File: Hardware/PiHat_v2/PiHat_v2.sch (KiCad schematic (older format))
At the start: 31 parts, among them P1 CONN_02X20, P2 CONN_01X02, P3 CONN_01X08

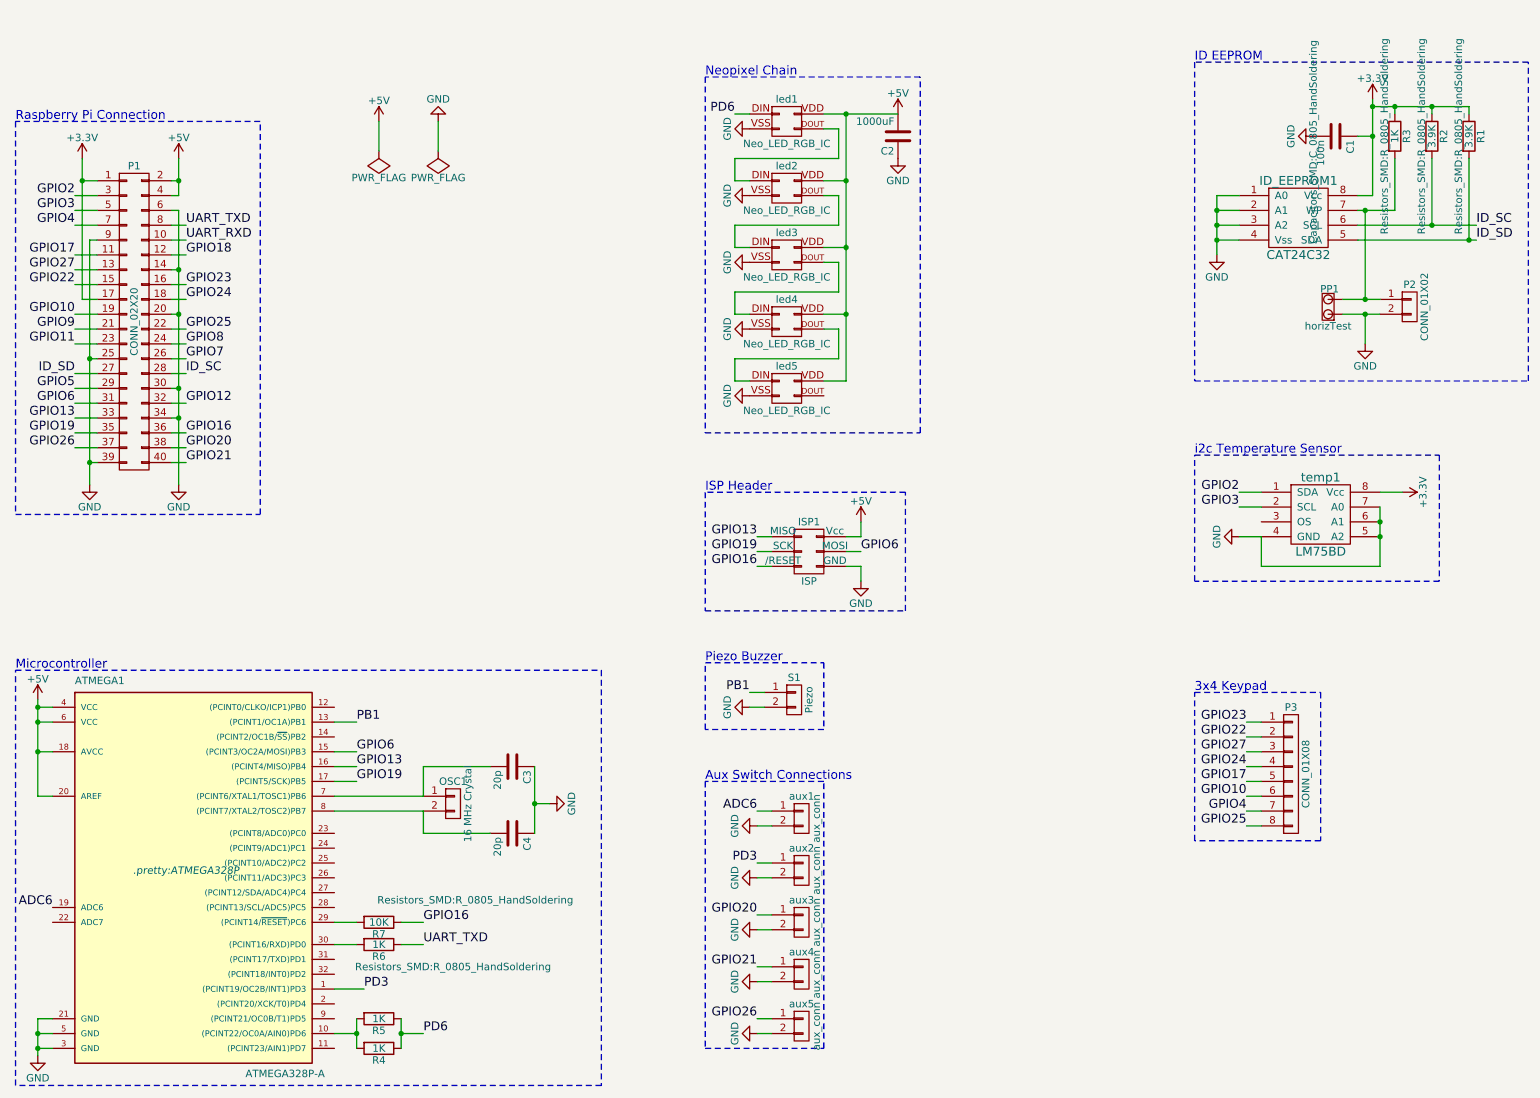
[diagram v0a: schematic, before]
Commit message: Take AREF off 5v for ATMEGA
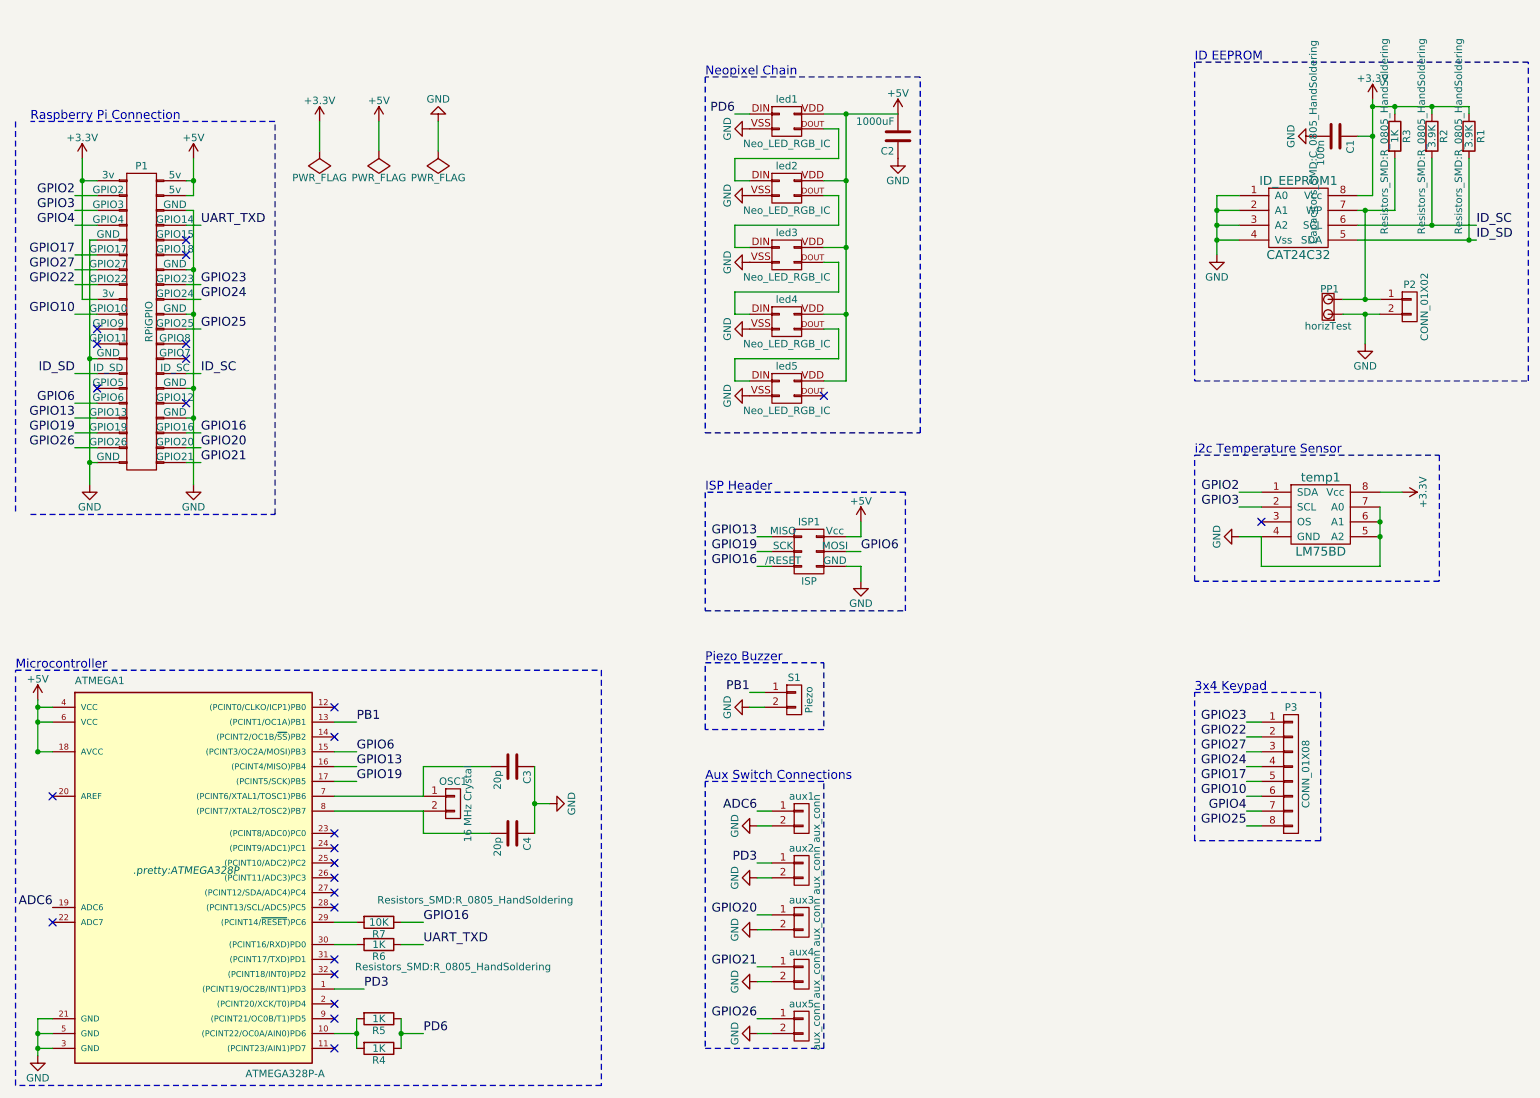
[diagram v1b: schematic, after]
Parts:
- removed P1: CONN_02X20, Pin_Headers:Pin_Header_Straight_2x20_Pitch2.54mm, symbol CONN_02X20
- added P1: RPiGPIO, symbol RPiGPIO
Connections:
- net +3V3: now also P1.1 (3v), P1.17 (3v)
- net +5V: now also P1.2 (5v), P1.4 (5v); no longer ATMEGA1.20 (AREF)
- net GND: now also P1.14 (GND), P1.20 (GND), P1.25 (GND), P1.30 (GND), P1.34 (GND), P1.39 (GND), P1.6 (GND), P1.9 (GND)
- net GPIO10: now also P1.19 (GPIO10)
- net GPIO13: now also P1.33 (GPIO13)
- net GPIO16: now also P1.36 (GPIO16)
- net GPIO17: now also P1.11 (GPIO17)
- net GPIO19: now also P1.35 (GPIO19)
- net GPIO2: now also P1.3 (GPIO2)
- net GPIO20: now also P1.38 (GPIO20)
- net GPIO21: now also P1.40 (GPIO21)
- net GPIO22: now also P1.15 (GPIO22)
- net GPIO23: now also P1.16 (GPIO23)
- net GPIO24: now also P1.18 (GPIO24)
- net GPIO25: now also P1.22 (GPIO25)
- net GPIO26: now also P1.37 (GPIO26)
- net GPIO27: now also P1.13 (GPIO27)
- net GPIO3: now also P1.5 (GPIO3)
- net GPIO4: now also P1.7 (GPIO4)
- net GPIO6: now also P1.31 (GPIO6)
- net ID_SC: now also P1.28 (ID_SC)
- net ID_SD: now also P1.27 (ID_SD)
- net UART_TXD: now also P1.8 (GPIO14)
- no-connect marks 0 -> 25
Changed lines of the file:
@@
 $EndDescr
-$Comp
-L CONN_02X20 P1
-U 1 1 588857EE
-P 1550 2500
-F 0 "P1" H 1550 3550 50  0000 C CNN
-F 1 "CONN_02X20" V 1550 2500 50  0000 C CNN
-F 2 "Pin_Headers:Pin_Header_Straight_2x20_Pitch2.54mm" H 1550 1550 50  0001 C CNN
-F 3 "" H 1550 1550 50  0000 C CNN
-	1    1550 2500
-	1    0    0    -1
-$EndComp
 $Comp
 L +3.3V #PWR01
@@
 L +5V #PWR02
 U 1 1 58885909
-P 1850 1400
-F 0 "#PWR02" H 1850 1250 50  0001 C CNN
-F 1 "+5V" H 1850 1540 50  0000 C CNN
-F 2 "" H 1850 1400 50  0000 C CNN
-F 3 "" H 1850 1400 50  0000 C CNN
-	1    1850 1400
+P 1950 1400
+F 0 "#PWR02" H 1950 1250 50  0001 C CNN
+F 1 "+5V" H 1950 1540 50  0000 C CNN
+F 2 "" H 1950 1400 50  0000 C CNN
+F 3 "" H 1950 1400 50  0000 C CNN
+	1    1950 1400
 	1    0    0    -1
 $EndComp
@@
 L GND #PWR03
 U 1 1 58885944
-P 1850 3600
-F 0 "#PWR03" H 1850 3350 50  0001 C CNN
-F 1 "GND" H 1850 3450 50  0000 C CNN
-F 2 "" H 1850 3600 50  0000 C CNN
-F 3 "" H 1850 3600 50  0000 C CNN
-	1    1850 3600
+P 1950 3600
+F 0 "#PWR03" H 1950 3350 50  0001 C CNN
+F 1 "GND" H 1950 3450 50  0000 C CNN
+F 2 "" H 1950 3600 50  0000 C CNN
+F 3 "" H 1950 3600 50  0000 C CNN
+	1    1950 3600
 	1    0    0    -1
 $EndComp
@@
 Text Label 1150 2450 2    60   ~ 0
 GPIO10
-Text Label 1150 2550 2    60   ~ 0
-GPIO9
-Text Label 1150 2650 2    60   ~ 0
-GPIO11
 Text Label 1150 2850 2    60   ~ 0
 ID_SD
-Text Label 1150 2950 2    60   ~ 0
-GPIO5
 Text Label 1150 3050 2    60   ~ 0
 GPIO6
@@
 Text Label 1150 3350 2    60   ~ 0
 GPIO26
-Text Label 1900 3450 0    60   ~ 0
+Text Label 2000 3450 0    60   ~ 0
 GPIO21
-Text Label 1900 3350 0    60   ~ 0
+Text Label 2000 3350 0    60   ~ 0
 GPIO20
-Text Label 1900 3250 0    60   ~ 0
+Text Label 2000 3250 0    60   ~ 0
 GPIO16
-Text Label 1900 3050 0    60   ~ 0
-GPIO12
-Text Label 1900 2850 0    60   ~ 0
+Text Label 2000 2850 0    60   ~ 0
 ID_SC
-Text Label 1900 2750 0    60   ~ 0
-GPIO7
-Text Label 1900 2650 0    60   ~ 0
-GPIO8
-Text Label 1900 2550 0    60   ~ 0
+Text Label 2000 2550 0    60   ~ 0
 GPIO25
-Text Label 1900 2350 0    60   ~ 0
+Text Label 2000 2350 0    60   ~ 0
 GPIO24
-Text Label 1900 2250 0    60   ~ 0
+Text Label 2000 2250 0    60   ~ 0
 GPIO23
-Text Label 1900 2050 0    60   ~ 0
-GPIO18
-Text Label 1900 1950 0    60   ~ 0
-UART_RXD
-Text Label 1900 1850 0    60   ~ 0
+Text Label 2000 1850 0    60   ~ 0
 UART_TXD
-Text Notes 750  1150 0    60   ~ 0
+Text Notes 850  1150 0    60   ~ 0
 Raspberry Pi Connection
 $Comp
@@
 	1000 7300 900  7300
 Connection ~ 900  5400
-Wire Wire Line
-	900  5700 1000 5700
 Connection ~ 900  5100
 Wire Wire Line
 	900  5400 1000 5400
-Wire Wire Line
-	900  5050 900  5700
 Wire Wire Line
 	1000 5100 900  5100
@@
 Wire Wire Line
 	1250 3450 1300 3450
-Connection ~ 1850 3150
-Connection ~ 1850 2950
-Connection ~ 1850 2450
-Connection ~ 1850 2150
-Wire Wire Line
-	1850 1750 1850 3600
-Wire Wire Line
-	1850 1750 1800 1750
-Wire Wire Line
-	1850 2150 1800 2150
-Wire Wire Line
-	1850 2450 1800 2450
-Wire Wire Line
-	1850 2950 1800 2950
-Wire Wire Line
-	1850 3150 1800 3150
-Wire Wire Line
-	1800 1550 1850 1550
-Wire Wire Line
-	1850 1400 1850 1650
-Wire Wire Line
-	1850 1650 1800 1650
-Connection ~ 1850 1550
+Connection ~ 1950 3150
+Connection ~ 1950 2950
+Connection ~ 1950 2450
+Connection ~ 1950 2150
+Wire Wire Line
+	1950 1750 1950 3600
+Wire Wire Line
+	1950 1750 1900 1750
+Wire Wire Line
+	1950 2150 1900 2150
+Wire Wire Line
+	1950 2450 1900 2450
+Wire Wire Line
+	1950 2950 1900 2950
+Wire Wire Line
+	1950 3150 1900 3150
+Wire Wire Line
+	1900 1550 1950 1550
+Wire Wire Line
+	1950 1400 1950 1650
+Wire Wire Line
+	1950 1650 1900 1650
+Connection ~ 1950 1550
 Wire Wire Line
 	1200 1400 1200 2350
@@
 	1150 2450 1300 2450
 Wire Wire Line
-	1300 2550 1150 2550
-Wire Wire Line
-	1150 2650 1300 2650
-Wire Wire Line
 	1300 2850 1150 2850
 Wire Wire Line
-	1150 2950 1300 2950
-Wire Wire Line
 	1300 3050 1150 3050
 Wire Wire Line
@@
 	1150 3350 1300 3350
 Wire Wire Line
-	1900 1850 1800 1850
-Wire Wire Line
-	1800 1950 1900 1950
-Wire Wire Line
-	1900 2050 1800 2050
-Wire Wire Line
-	1800 2250 1900 2250
-Wire Wire Line
-	1900 2350 1800 2350
-Wire Wire Line
-	1800 2550 1900 2550
-Wire Wire Line
-	1900 2650 1800 2650
-Wire Wire Line
-	1800 2750 1900 2750
-Wire Wire Line
-	1900 2850 1800 2850
-Wire Wire Line
-	1800 3050 1900 3050
-Wire Wire Line
-	1900 3250 1800 3250
-Wire Wire Line
-	1800 3350 1900 3350
-Wire Wire Line
-	1900 3450 1800 3450
+	2000 1850 1900 1850
+Wire Wire Line
+	1900 2250 2000 2250
+Wire Wire Line
+	2000 2350 1900 2350
+Wire Wire Line
+	1900 2550 2000 2550
+Wire Wire Line
+	2000 2850 1900 2850
+Wire Wire Line
+	2000 3250 1900 3250
+Wire Wire Line
+	1900 3350 2000 3350
+Wire Wire Line
+	2000 3450 1900 3450
 Wire Wire Line
 	9800 1950 10600 1950
@@
 Connection ~ 3350 7300
 Wire Notes Line
-	750  3800 2400 3800
-Wire Notes Line
-	2400 3800 2400 1150
-Wire Notes Line
-	2400 1150 750  1150
+	850  3800 2500 3800
+Wire Notes Line
+	2500 3800 2500 1150
+Wire Notes Line
+	2500 1150 850  1150
 Wire Wire Line
 	6350 4150 6450 4150
@@
 	1    0    0    -1
 $EndComp
+$Comp
+L RPiGPIO P1
+U 1 1 59470B68
+P 1600 2500
+F 0 "P1" H 1600 3550 50  0000 C CNN
+F 1 "RPiGPIO" V 1650 2500 50  0000 C CNN
+F 2 "" H 1650 1550 50  0000 C CNN
+F 3 "" H 1650 1550 50  0000 C CNN
+	1    1600 2500
+	1    0    0    -1
+$EndComp
+$Comp
+L +3.3V #PWR033
+U 1 1 5947169C
+P 2800 1150
+F 0 "#PWR033" H 2800 1000 50  0001 C CNN
+F 1 "+3.3V" H 2800 1290 50  0000 C CNN
+F 2 "" H 2800 1150 50  0000 C CNN
+F 3 "" H 2800 1150 50  0000 C CNN
+	1    2800 1150
+	1    0    0    -1
+$EndComp
+$Comp
+L PWR_FLAG #FLG034
+U 1 1 594716EE
+P 2800 1350
+F 0 "#FLG034" H 2800 1445 50  0001 C CNN
+F 1 "PWR_FLAG" H 2800 1530 50  0000 C CNN
+F 2 "" H 2800 1350 50  0000 C CNN
+F 3 "" H 2800 1350 50  0000 C CNN
+	1    2800 1350
+	-1   0    0    1
+$EndComp
+Wire Wire Line
+	2800 1150 2800 1350
+NoConn ~ 1300 2550
+NoConn ~ 1300 2650
+NoConn ~ 1300 2950
+NoConn ~ 1900 3050
+NoConn ~ 1900 2750
+NoConn ~ 1900 2650
+NoConn ~ 1900 2050
+NoConn ~ 1900 1950
+NoConn ~ 2900 5950
+NoConn ~ 2900 6050
+NoConn ~ 2900 6150
+NoConn ~ 2900 6250
+NoConn ~ 2900 6350
+NoConn ~ 2900 6450
+NoConn ~ 2900 6800
+NoConn ~ 2900 6900
+NoConn ~ 2900 7100
+NoConn ~ 2900 7200
+NoConn ~ 2900 7400
+NoConn ~ 2900 5300
+NoConn ~ 2900 5100
+NoConn ~ 1000 6550
+NoConn ~ 9150 3850
+NoConn ~ 6200 3000
+NoConn ~ 1000 5700
+Wire Wire Line
+	900  5400 900  5050
 $EndSCHEMATC

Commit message: Adjust Schematic Styling
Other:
- note added: "PWR_FLAGS"
- moved on the sheet: C1, ID_EEPROM1, P1, P2, P3, PP1, R1, R2, R3, S1, temp1

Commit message: Update Footprints
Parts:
- C3, C4: footprint Capacitors_THT:C_Disc_D5.0mm_W2.5mm_P2.50mm -> Capacitors_SMD:C_0603_HandSoldering
- ISP1: footprint (none) -> Pin_Headers:Pin_Header_Straight_2x03_Pitch2.54mm
- OSC1: footprint Crystals:Resonator-2pin_w10.0mm_h5.0mm -> Crystals:Crystal_SMD_HC49-SD_HandSoldering
- P1: footprint (none) -> Pin_Headers:Pin_Header_Straight_2x20_Pitch1.27mm
- R4, R5: footprint (none) -> Resistors_SMD:R_0805_HandSoldering
- aux1, aux2, aux3, aux4, aux5: footprint (none) -> Pin_Headers:Pin_Header_Straight_1x02_Pitch2.54mm
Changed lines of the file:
@@
 F 0 "OSC1" H 3700 5900 50  0000 C CNN
 F 1 "16 MHz Crystal" V 3800 5750 50  0000 C CNN
-F 2 "Crystals:Resonator-2pin_w10.0mm_h5.0mm" H 3700 5750 50  0001 C CNN
+F 2 "Crystals:Crystal_SMD_HC49-SD_HandSoldering" H 3700 5750 50  0001 C CNN
 F 3 "" H 3700 5750 50  0000 C CNN
 	1    3700 5750
@@
 F 0 "C3" H 4125 5600 50  0000 L CNN
 F 1 "20p" H 4125 5400 50  0000 L CNN
-F 2 "Capacitors_THT:C_Disc_D5.0mm_W2.5mm_P2.50mm" H 4138 5350 50  0001 C CNN
+F 2 "Capacitors_SMD:C_0603_HandSoldering" H 4138 5350 50  0001 C CNN
 F 3 "" H 4100 5500 50  0000 C CNN
 	1    4100 5500
@@
 F 0 "C4" H 4125 6050 50  0000 L CNN
 F 1 "20p" H 4125 5850 50  0000 L CNN
-F 2 "Capacitors_THT:C_Disc_D5.0mm_W2.5mm_P2.50mm" H 4138 5800 50  0001 C CNN
+F 2 "Capacitors_SMD:C_0603_HandSoldering" H 4138 5800 50  0001 C CNN
 F 3 "" H 4100 5950 50  0000 C CNN
 	1    4100 5950
@@
 F 0 "R5" V 3280 7200 50  0000 C CNN
 F 1 "1K" V 3200 7200 50  0000 C CNN
-F 2 "" V 3130 7200 50  0000 C CNN
+F 2 "Resistors_SMD:R_0805_HandSoldering" V 3130 7200 50  0001 C CNN
 F 3 "" H 3200 7200 50  0000 C CNN
 	1    3200 7200
@@
 F 0 "R4" V 3280 7400 50  0000 C CNN
 F 1 "1K" V 3200 7400 50  0000 C CNN
-F 2 "" V 3130 7400 50  0000 C CNN
+F 2 "Resistors_SMD:R_0805_HandSoldering" V 3130 7400 50  0001 C CNN
 F 3 "" H 3200 7400 50  0000 C CNN
 	1    3200 7400
@@
 F 0 "ISP1" H 6100 4250 50  0000 C CNN
 F 1 "ISP" H 6100 3850 50  0000 C CNN
-F 2 "" H 6100 2850 50  0000 C CNN
+F 2 "Pin_Headers:Pin_Header_Straight_2x03_Pitch2.54mm" H 6100 2850 50  0001 C CNN
 F 3 "" H 6100 2850 50  0000 C CNN
 	1    6100 4050
@@
 F 0 "aux1" H 6050 6000 50  0000 C CNN
 F 1 "aux_conn" V 6150 5850 50  0000 C CNN
-F 2 "" H 6050 5850 50  0000 C CNN
+F 2 "Pin_Headers:Pin_Header_Straight_1x02_Pitch2.54mm" H 6050 5850 50  0001 C CNN
 F 3 "" H 6050 5850 50  0000 C CNN
 	1    6050 5850
@@
 F 0 "aux2" H 6050 6350 50  0000 C CNN
 F 1 "aux_conn" V 6150 6200 50  0000 C CNN
-F 2 "" H 6050 6200 50  0000 C CNN
+F 2 "Pin_Headers:Pin_Header_Straight_1x02_Pitch2.54mm" H 6050 6200 50  0001 C CNN
 F 3 "" H 6050 6200 50  0000 C CNN
 	1    6050 6200
@@
 F 0 "aux3" H 6050 6700 50  0000 C CNN
 F 1 "aux_conn" V 6150 6550 50  0000 C CNN
-F 2 "" H 6050 6550 50  0000 C CNN
+F 2 "Pin_Headers:Pin_Header_Straight_1x02_Pitch2.54mm" H 6050 6550 50  0001 C CNN
 F 3 "" H 6050 6550 50  0000 C CNN
 	1    6050 6550
@@
 F 0 "aux4" H 6050 7050 50  0000 C CNN
 F 1 "aux_conn" V 6150 6900 50  0000 C CNN
-F 2 "" H 6050 6900 50  0000 C CNN
+F 2 "Pin_Headers:Pin_Header_Straight_1x02_Pitch2.54mm" H 6050 6900 50  0001 C CNN
 F 3 "" H 6050 6900 50  0000 C CNN
 	1    6050 6900
@@
 F 0 "aux5" H 6050 7400 50  0000 C CNN
 F 1 "aux_conn" V 6150 7250 50  0000 C CNN
-F 2 "" H 6050 7250 50  0000 C CNN
+F 2 "Pin_Headers:Pin_Header_Straight_1x02_Pitch2.54mm" H 6050 7250 50  0001 C CNN
 F 3 "" H 6050 7250 50  0000 C CNN
 	1    6050 7250
@@
 F 0 "P1" H 1650 3250 50  0000 C CNN
 F 1 "RPiGPIO" V 1700 2200 50  0000 C CNN
-F 2 "" H 1700 1250 50  0000 C CNN
+F 2 "Pin_Headers:Pin_Header_Straight_2x20_Pitch1.27mm" H 1700 1250 50  0001 C CNN
 F 3 "" H 1700 1250 50  0000 C CNN
 	1    1650 2200

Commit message: Correct RPiGPIO and Crystal Footprints
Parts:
- OSC1: footprint Crystals:Crystal_SMD_HC49-SD_HandSoldering -> Crystals:Crystal_SMD_HC49-SD
- P1: footprint Pin_Headers:Pin_Header_Straight_2x20_Pitch1.27mm -> Pin_Headers:Pin_Header_Straight_2x20_Pitch2.54mm
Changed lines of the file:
@@
 F 0 "OSC1" H 3700 5900 50  0000 C CNN
 F 1 "16 MHz Crystal" V 3800 5750 50  0000 C CNN
-F 2 "Crystals:Crystal_SMD_HC49-SD_HandSoldering" H 3700 5750 50  0001 C CNN
+F 2 "Crystals:Crystal_SMD_HC49-SD" H 3700 5750 50  0001 C CNN
 F 3 "" H 3700 5750 50  0000 C CNN
 	1    3700 5750
@@
 F 0 "P1" H 1650 3250 50  0000 C CNN
 F 1 "RPiGPIO" V 1700 2200 50  0000 C CNN
-F 2 "Pin_Headers:Pin_Header_Straight_2x20_Pitch1.27mm" H 1700 1250 50  0001 C CNN
+F 2 "Pin_Headers:Pin_Header_Straight_2x20_Pitch2.54mm" H 1700 1250 50  0001 C CNN
 F 3 "" H 1700 1250 50  0000 C CNN
 	1    1650 2200

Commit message: Move to SMT Piezo Buzzer
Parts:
- S1: footprint .pretty:PKM13EPYH -> .pretty:Piezo_CT-1205h-smt
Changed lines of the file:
@@
 F 0 "S1" H 6000 5250 50  0000 C CNN
 F 1 "Piezo" V 6100 5100 50  0000 C CNN
-F 2 ".pretty:PKM13EPYH" H 6000 5100 50  0001 C CNN
+F 2 ".pretty:Piezo_CT-1205h-smt" H 6000 5100 50  0001 C CNN
 F 3 "" H 6000 5100 50  0000 C CNN
 	1    6000 5100

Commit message: Implement Mounting Holes in Schematic for Netlist Use
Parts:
- added MountHole1, MountHole2, MountHole3, MountHole4: CONN_01X01, .pretty:raspiMountingHole, symbol CONN_01X01
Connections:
- no-connect marks 25 -> 29
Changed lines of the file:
@@
 Wire Notes Line
 	850  850  850  3500
+$Comp
+L CONN_01X01 MountHole2
+U 1 1 59476266
+P 3900 2150
+F 0 "MountHole2" H 3900 2250 50  0000 C CNN
+F 1 "CONN_01X01" V 4000 2150 50  0000 C CNN
+F 2 ".pretty:raspiMountingHole" H 3900 2150 50  0001 C CNN
+F 3 "" H 3900 2150 50  0000 C CNN
+	1    3900 2150
+	1    0    0    -1
+$EndComp
+$Comp
+L CONN_01X01 MountHole4
+U 1 1 594763CB
+P 3900 2650
+F 0 "MountHole4" H 3900 2750 50  0000 C CNN
+F 1 "CONN_01X01" V 4000 2650 50  0000 C CNN
+F 2 ".pretty:raspiMountingHole" H 3900 2650 50  0001 C CNN
+F 3 "" H 3900 2650 50  0000 C CNN
+	1    3900 2650
+	1    0    0    -1
+$EndComp
+$Comp
+L CONN_01X01 MountHole1
+U 1 1 59476454
+P 3350 2150
+F 0 "MountHole1" H 3350 2250 50  0000 C CNN
+F 1 "CONN_01X01" V 3450 2150 50  0000 C CNN
+F 2 ".pretty:raspiMountingHole" H 3350 2150 50  0001 C CNN
+F 3 "" H 3350 2150 50  0000 C CNN
+	1    3350 2150
+	-1   0    0    1
+$EndComp
+$Comp
+L CONN_01X01 MountHole3
+U 1 1 594764EA
+P 3350 2650
+F 0 "MountHole3" H 3350 2750 50  0000 C CNN
+F 1 "CONN_01X01" V 3450 2650 50  0000 C CNN
+F 2 ".pretty:raspiMountingHole" H 3350 2650 50  0001 C CNN
+F 3 "" H 3350 2650 50  0000 C CNN
+	1    3350 2650
+	-1   0    0    1
+$EndComp
+NoConn ~ 3550 2150
+NoConn ~ 3700 2150
+NoConn ~ 3700 2650
+NoConn ~ 3550 2650
 $EndSCHEMATC

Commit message: Route all traces on PCB
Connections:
- no-connect marks 29 -> 30
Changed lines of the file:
@@
 NoConn ~ 3700 2650
 NoConn ~ 3550 2650
+NoConn ~ 3800 2750
 $EndSCHEMATC
